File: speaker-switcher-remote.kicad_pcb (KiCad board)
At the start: 2 copper layers, 49.8 x 60 mm, 21 parts, among them M1 arduino-nano, Q1 TIP31C, Q2 TIP31C

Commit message: Reworking pcb
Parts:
- added C1: .33uF, Capacitor_THT:CP_Radial_D10.0mm_P5.00mm, F.Cu at (111.2, 34.5)
- added C2: .1uF, Capacitor_THT:CP_Radial_D10.0mm_P5.00mm, F.Cu at (123.1, 34.5)
- added C3: 100uF, Capacitor_THT:CP_Radial_D10.0mm_P5.00mm, F.Cu at (134.9, 34.5)
- added U1: LM7805_TO220, Package_TO_SOT_THT:TO-220-3_Vertical, F.Cu at (110.9, 44.2)
- moved REF** 80.3 mm to (69.2, 18.4)
- moved REF** 80.3 mm to (25.2, 18.4)
- moved IR1 75.8 mm to (49.3, 27.0)
- moved R2 75.8 mm to (54.2, 33.1)
- moved R3 75.8 mm to (59.5, 53.9)
- moved R4 75.8 mm to (46.8, 38.6)
- moved R5 75.8 mm to (46.8, 53.6)
- moved R7 75.8 mm to (65.2, 53.6)
- moved M1 75.8 mm to (34.1, 53.7)
- moved OUT+1 75.8 mm to (65.1, 69.0)
- moved OUT-1 75.8 mm to (64.5, 77.8)
- moved PWR+1 75.8 mm to (49.3, 69.0)
- moved PWR-1 75.8 mm to (48.8, 77.8)
- moved Q1 75.8 mm to (48.0, 60.4)
- moved Q2 75.8 mm to (60.0, 60.4)
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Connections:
- net /OUT+ renamed Net-(D1-Pad1)
- net /OUT- renamed Net-(D1-Pad2)
- IR1 pad 3: Net-(IR1-Pad3) -> Net-(C3-Pad1)
- M1 pad 2: Net-(IR1-Pad3) -> Net-(M1-Pad2)
- R6 pad 2: Net-(M1-Pad22) -> Net-(Q1-Pad2)
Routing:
- net GNDREF: track 101.1 -> 0.44 mm
- net PWR: track 46.7 -> 0.85 mm
- net +5V: track 32.1 -> 0.00 mm
- net Net-(Q2-Pad1): track 29.6 -> 0.71 mm
- net Net-(R6-Pad1): track 30.1 -> 2.77 mm
- net Net-(Q1-Pad1): track 25.4 -> 0.00 mm
- net Net-(IR1-Pad3): track 22.5 -> 0.00 mm
- net Net-(D1-Pad2): track 22.3 -> 1.01 mm
- net Net-(M1-Pad22): track 20.9 -> 0.00 mm
- net Net-(D1-Pad1): track 19.3 -> 0.00 mm
- net Net-(M1-Pad20): track 15.3 -> 0.34 mm
- net Net-(IR1-Pad1): track 13.6 -> 0.00 mm
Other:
- board size 49.8 x 60 mm -> 50 x 70 mm

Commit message: Updated board
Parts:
- removed R4, R5: 1k, Resistor_THT:R_Axial_DIN0207_L6.3mm_D2.5mm_P7.62mm_Horizontal
- added C4: 100pF, Capacitor_THT:C_Disc_D6.0mm_W2.5mm_P5.00mm, F.Cu at (157.8, 87.5)
- added D1: 1N4148, Diode_THT:D_DO-41_SOD81_P3.81mm_Vertical_KathodeUp, F.Cu at (166.2, 117.5)
- added R10: 100, Resistor_THT:R_Axial_DIN0207_L6.3mm_D2.5mm_P2.54mm_Vertical, F.Cu at (128.2, 76.0)
- added R8: 100, Resistor_THT:R_Axial_DIN0207_L6.3mm_D2.5mm_P2.54mm_Vertical, F.Cu at (133.2, 76.0)
- added R9: 47k, Resistor_THT:R_Axial_DIN0207_L6.3mm_D2.5mm_P2.54mm_Vertical, F.Cu at (133.2, 68.0)
- C1, C2, C3: footprint Capacitor_THT:CP_Radial_D10.0mm_P5.00mm -> Capacitor_THT:CP_Radial_D10.0mm_P2.50mm
- Q1: value TIP31C -> 2N2222; footprint Package_TO_SOT_THT:TO-220-3_Vertical -> Package_TO_SOT_THT:TO-92
- R1, R2, R3, R6: footprint Resistor_THT:R_Axial_DIN0207_L6.3mm_D2.5mm_P7.62mm_Horizontal -> Resistor_THT:R_Axial_DIN0207_L6.3mm_D2.5mm_P2.54mm_Vertical
- moved REF** 149.0 mm to (166.2, 66.5)
- moved REF** 148.3 mm to (166.2, 126.5)
- moved IR1 137.7 mm to (167.2, 98.0), turned to 0 degrees
- moved R1 120.9 mm to (161.2, 82.5), turned to 180 degrees
- moved M1 116.8 mm to (145.8, 88.0)
- moved R2 115.8 mm to (161.2, 77.5)
- moved R3 114.5 mm to (166.8, 94.0)
- moved R7 111.1 mm to (157.2, 116.0), turned to 180 degrees
- moved OUT+1 110.9 mm to (160.6, 125.2), turned to 90 degrees
- moved SIG+1 107.6 mm to (149.2, 125.2), turned to 90 degrees
- moved Q2 107.4 mm to (160.2, 99.0), turned to 90 degrees
- moved PWR+1 103.7 mm to (136.5, 125.2), turned to 90 degrees
- moved OUT-1 102.6 mm to (155.5, 125.2), turned to 90 degrees
- moved SIG-1 99.7 mm to (144.1, 125.2), turned to 90 degrees
- moved PWR-1 95.2 mm to (131.4, 125.2), turned to 270 degrees
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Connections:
- Q1 pad 1: Net-(Q1-Pad1) -> Net-(M1-Pad22)
- Q1 pad 2: PWR -> Net-(Q1-Pad2)
- Q1 pad 3: +5V -> Net-(Q1-Pad3)
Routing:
- net GNDREF: track 0.44 -> 136.4 mm
- net Net-(C3-Pad1): track 0.00 -> 70.1 mm
- net +5V: track 0.00 -> 67.3 mm
- net Net-(IR1-Pad1): track 0.00 -> 55.4 mm
- net Net-(R6-Pad1): track 2.77 -> 56.3 mm
- net PWR: track 0.85 -> 51.4 mm
- net Net-(D1-Pad2): track 1.01 -> 40.3 mm
- net Net-(Q2-Pad1): track 0.71 -> 28.5 mm
- net Net-(M1-Pad22): track 0.00 -> 27.5 mm
- net Net-(D1-Pad1): track 0.00 -> 21.7 mm
- net Net-(Q1-Pad3): track 0.00 -> 9.53 mm
- net Net-(M1-Pad2): track 0.00 -> 8.09 mm
- net Net-(Q1-Pad2): track 0.00 -> 6.46 mm
- net Net-(M1-Pad20): track 0.34 -> 6.53 mm

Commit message: New PCB layout
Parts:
- moved IR1 33.2 mm to (160.2, 65.5)
- moved R2 20.2 mm to (164.2, 97.5), turned to 90 degrees
- moved C3 19.9 mm to (159.9, 88.1)
- moved R1 17.9 mm to (160.0, 100.4), turned to 90 degrees
- moved C4 10.9 mm to (158.1, 76.6)
- moved Q2 10.8 mm to (165.1, 108.6), turned to 180 degrees
- moved R3 7.72 mm to (164.2, 101.3), turned to 270 degrees
- moved R10 1.87 mm to (126.6, 76.9), turned to 0 degrees
- moved R8 0.64 mm to (133.2, 76.6)
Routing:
- net Net-(C3-Pad1): track 70.1 -> 44.0 mm
- net Net-(IR1-Pad1): track 55.4 -> 31.2 mm
- net Net-(D1-Pad2): track 40.3 -> 23.0 mm
- net Net-(Q2-Pad1): track 28.5 -> 13.5 mm
- net Net-(M1-Pad20): track 6.53 -> 20.4 mm
- net GNDREF: track 136.4 -> 145.1 mm
- net Net-(M1-Pad22): track 27.5 -> 36.1 mm
- net Net-(Q1-Pad3): track 9.53 -> 5.81 mm
- net +5V: track 67.3 -> 64.8 mm

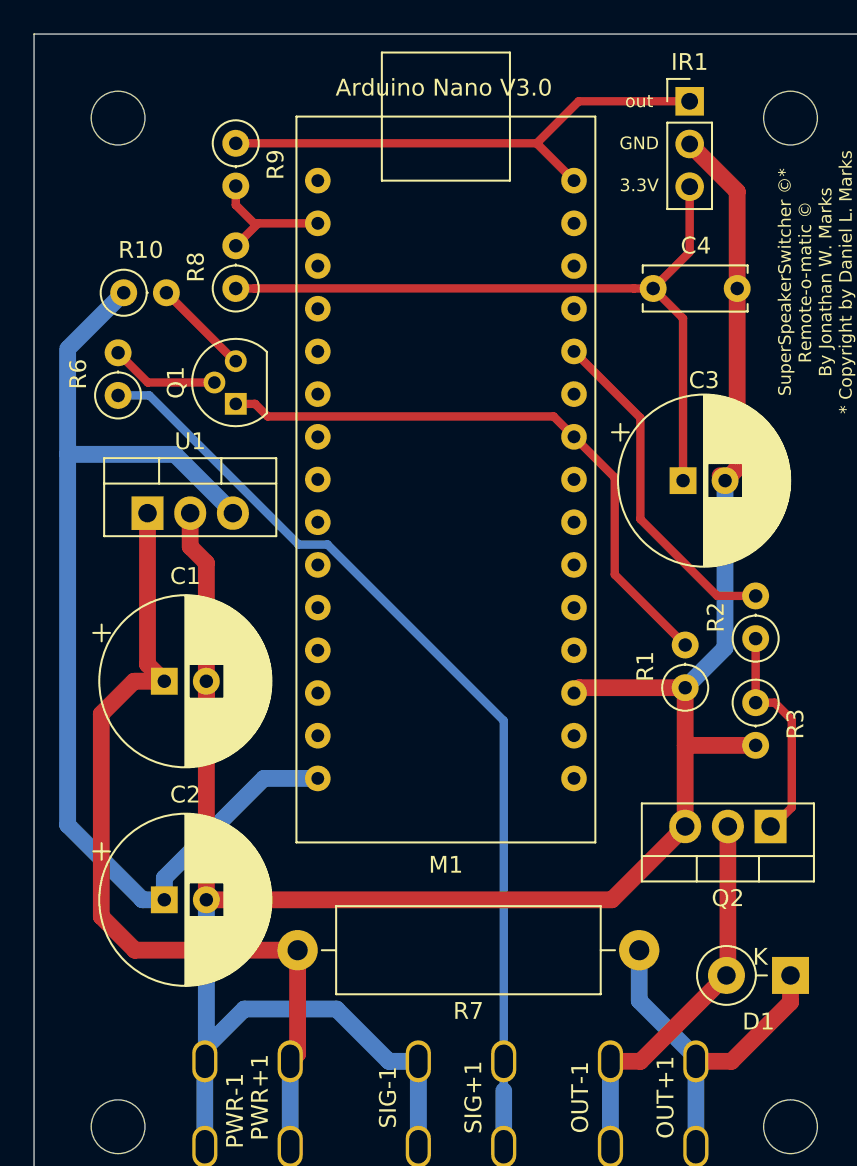
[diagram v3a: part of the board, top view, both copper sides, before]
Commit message: Stabilize signal input
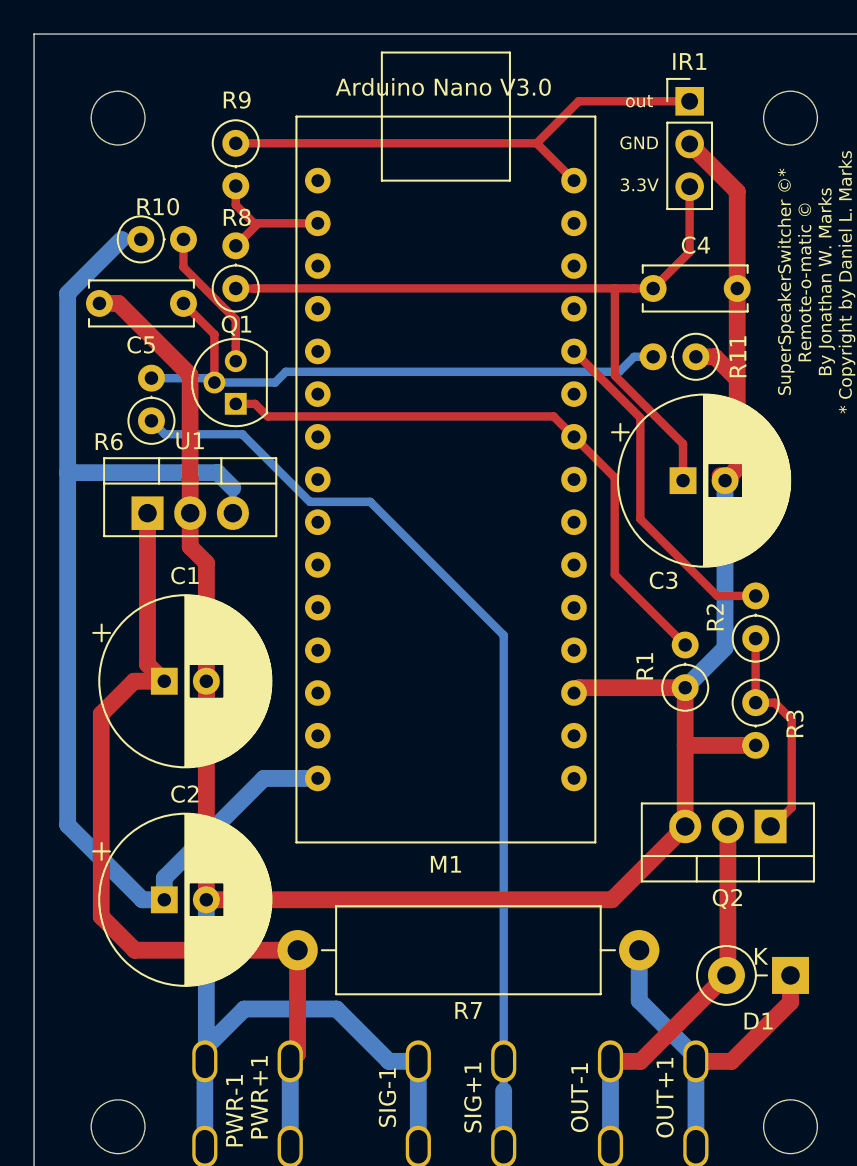
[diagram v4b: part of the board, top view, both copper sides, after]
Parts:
- added C5: 100pF, Capacitor_THT:C_Disc_D6.0mm_W2.5mm_P5.00mm, F.Cu at (130.1, 77.5)
- added R11: 100k, Resistor_THT:R_Axial_DIN0207_L6.3mm_D2.5mm_P2.54mm_Vertical, F.Cu at (160.6, 80.7)
- moved R10 3.33 mm to (127.6, 73.7)
- moved R6 2.49 mm to (128.2, 84.5)
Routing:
- net Net-(C5-Pad1): track 6.46 -> 36.1 mm
- net GNDREF: track 145.1 -> 163.4 mm
- net +5V: track 64.8 -> 69.5 mm
- net Net-(Q1-Pad3): track 5.81 -> 9.32 mm
- net Net-(C3-Pad1): track 44.0 -> 44.9 mm

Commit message: Updated PCB but not plots
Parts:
- removed the REF** at (166.2, 126.5)
- removed the REF** at (126.2, 126.5)
- removed the REF** at (126.2, 66.5)
- removed the REF** at (166.2, 66.5)
- added REF**: MountingHole_3mm, MountingHole:MountingHole_3mm, F.Cu at (190.2, 71.5)
- added REF**: MountingHole_3mm, MountingHole:MountingHole_3mm, F.Cu at (107.2, 71.5)
- added REF**: MountingHole_3mm, MountingHole:MountingHole_3mm, F.Cu at (107.2, 124.5)
- added REF**: MountingHole_3mm, MountingHole:MountingHole_3mm, F.Cu at (190.2, 124.5)
- D1: footprint Diode_THT:D_DO-41_SOD81_P3.81mm_Vertical_KathodeUp -> Diode_THT:D_DO-41_SOD81_P7.62mm_Horizontal
- R1, R10, R11, R2, R3, R6, R8, R9: footprint Resistor_THT:R_Axial_DIN0207_L6.3mm_D2.5mm_P2.54mm_Vertical -> Resistor_THT:R_Axial_DIN0207_L6.3mm_D2.5mm_P7.62mm_Horizontal
- moved R10 47.1 mm to (154.2, 112.5), turned to 90 degrees
- moved R6 44.1 mm to (162.2, 112.5)
- moved U1 33.1 mm to (114.0, 120.0)
- moved C5 32.4 mm to (162.2, 81.5), turned to 0 degrees
- moved Q1 28.7 mm to (158.2, 97.5), turned to 0 degrees
- moved R9 23.0 mm to (117.2, 84.5), turned to 90 degrees
- moved C2 21.9 mm to (117.2, 94.5), turned to 180 degrees
- moved OUT+1 19.2 mm to (179.8, 125.5), turned to 0 degrees
- moved M1 18.2 mm to (132.0, 100.0)
- moved C1 17.5 mm to (114.0, 109.0)
- moved D1 15.0 mm to (181.2, 118.5)
- moved R1 14.7 mm to (145.2, 100.5), turned to 0 degrees
- moved PWR-1 13.2 mm to (118.2, 125.5), turned to 0 degrees
- moved OUT-1 12.3 mm to (167.8, 125.5), turned to 0 degrees
- moved R8 12.1 mm to (145.2, 78.5), turned to 270 degrees
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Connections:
- R9 pad 1: Net-(IR1-Pad1) -> Net-(M1-Pad2)
- R9 pad 2: Net-(M1-Pad2) -> Net-(IR1-Pad1)
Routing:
- net GNDREF: track 163.4 -> 224.9 mm
- net Net-(R6-Pad1): track 56.7 -> 19.9 mm
- net Net-(M1-Pad2): track 8.35 -> 28.7 mm
- net Net-(IR1-Pad1): track 31.2 -> 44.1 mm
- net Net-(M1-Pad22): track 36.1 -> 23.5 mm
- net Net-(C5-Pad1): track 36.1 -> 26.0 mm
- net Net-(D1-Pad1): track 21.7 -> 31.0 mm
- net Net-(M1-Pad20): track 20.4 -> 28.8 mm
- net Net-(C3-Pad1): track 44.9 -> 38.3 mm
- net +5V: track 69.5 -> 64.5 mm
- net PWR: track 51.4 -> 47.5 mm
- net Net-(D1-Pad2): track 23.0 -> 20.5 mm
- net Net-(Q2-Pad1): track 13.5 -> 15.2 mm
- net Net-(Q1-Pad3): track 9.32 -> 10.1 mm
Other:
- board size 50 x 70 mm -> 91 x 60 mm
- board text added: "SuperSpeakerSwitcher © Dr. Daniel Marks Speaker Switcher Remote © by Jonathan Marks"
- board text added: "https://github.com/reddevil578/speaker-switcher-remote"
- board text removed: "3.3V"
- board text removed: "Arduino Nano V3.0"
- board text removed: "GND"
- board text removed: "SuperSpeakerSwitcher ©* Remote-o-matic © By Jonathan W. Marks * Copyright by Daniel L. Marks"
- board text removed: "out"
